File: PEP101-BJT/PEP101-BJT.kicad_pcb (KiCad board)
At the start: 2 copper layers, 45 x 45 mm, 14 parts, among them J1 Screw_Terminal_01x02, J2 Screw_Terminal_01x02, J3 Screw_Terminal_01x02, Q2 MMBT5551L

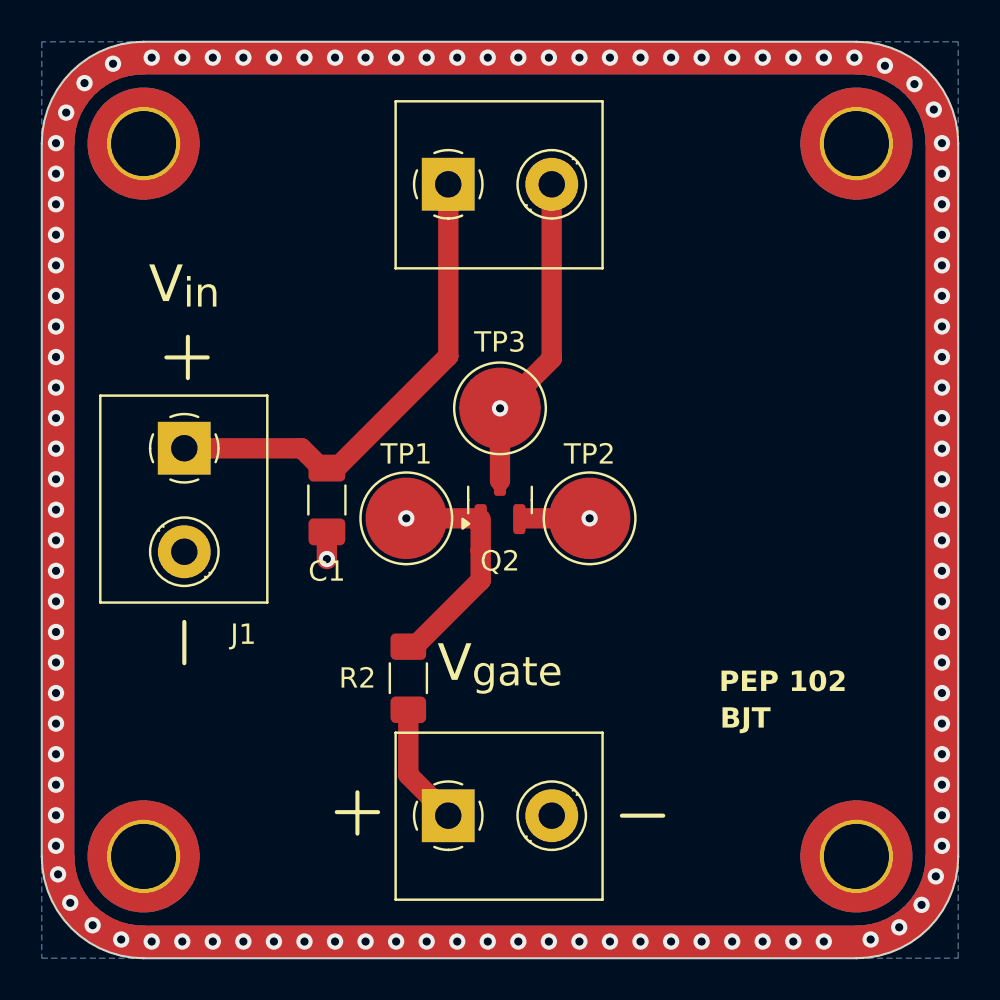
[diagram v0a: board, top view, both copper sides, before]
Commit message: bjt and mosfet need to be redesigned.
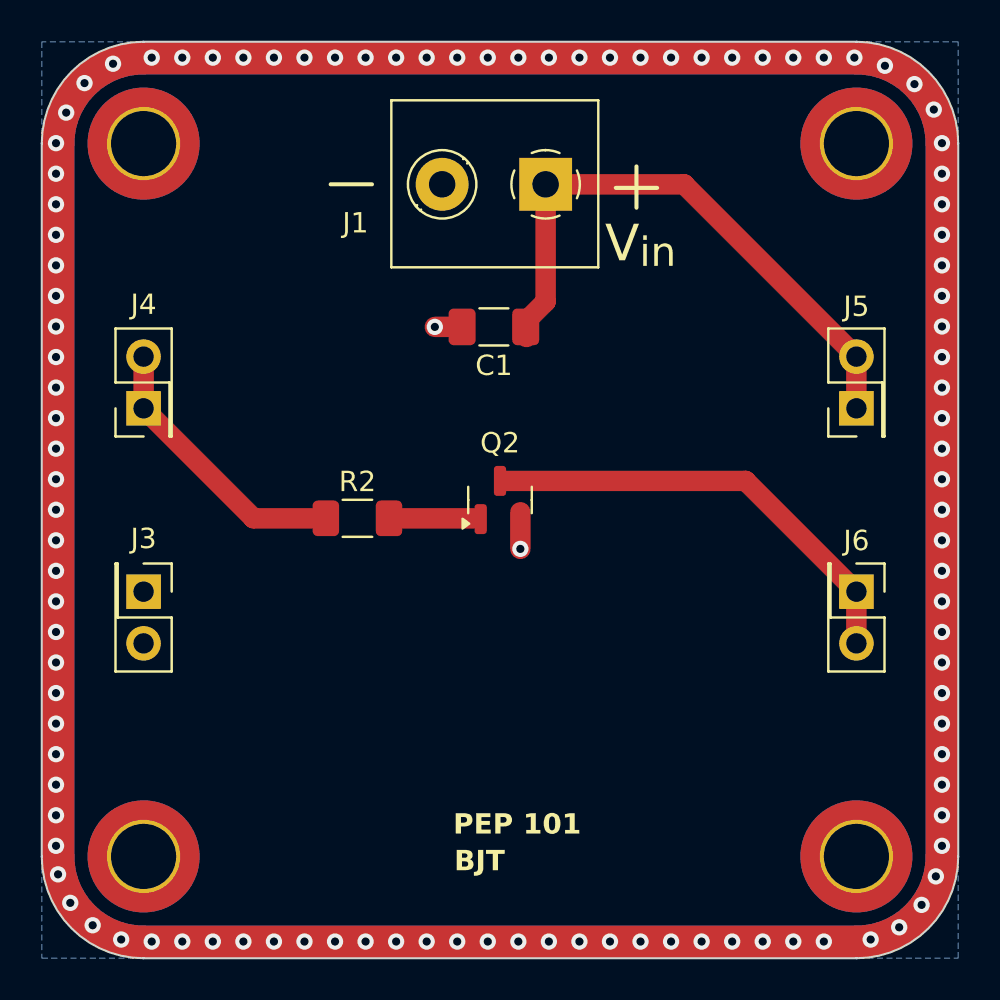
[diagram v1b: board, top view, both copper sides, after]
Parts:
- removed J2: Screw_Terminal_01x02, PEP_library:Screw terminal
- removed REF**: R_silk_symbol, PEP:R_silk_symbol
- removed TP1, TP2, TP3: TestPoint, TestPoint:TestPoint_Pad_D4.0mm
- added J4: Conn_01x02_Pin, Connector_PinHeader_2.54mm:PinHeader_2x01_P2.54mm_Vertical, F.Cu at (105.0, 118.0)
- added J5: Conn_01x02_Pin, Connector_PinHeader_2.54mm:PinHeader_2x01_P2.54mm_Vertical, F.Cu at (140.0, 118.0)
- added J6: Conn_01x02_Pin, Connector_PinHeader_2.54mm:PinHeader_2x01_P2.54mm_Vertical, F.Cu at (140.0, 127.0)
- J3: value Screw_Terminal_01x02 -> Conn_01x02_Pin; footprint PEP_library:TerminalBlock_Phoenix_MKDS-1,5-2-5.08_1x02_P5.08mm_Horizontal -> Connector_PinHeader_2.54mm:PinHeader_2x01_P2.54mm_Vertical
- moved J1 21.7 mm to (122.2, 107.0), turned to 180 degrees
- moved J3 20.7 mm to (105.0, 127.0), turned to -90 degrees
- moved C1 11.8 mm to (122.2, 114.0), turned to 180 degrees
- moved R2 8.24 mm to (115.5, 123.4), turned to 0 degrees
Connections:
- J3 pad 1: BASE -> 0
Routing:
- net BASE: track 5.89 -> 13.9 mm
- net Net-(Q2-B): track 10.7 -> 4.00 mm, vias 1 -> 0
- net Net-(J6-Pin_1): track 15.7 -> 22.1 mm, vias 1 -> 0
- net VCC: track 24.2 -> 29.9 mm
- net 0: track 4.40 -> 3.00 mm
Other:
- board text added: "PEP 101"
- board text removed: "PEP 102"

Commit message: Nova estetika.
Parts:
- added REF**: R_silk_symbol, PEP_library:R_silk_symbol, F.Cu at (110.1, 116.8)
- added REF**: C_silk_symbol, PEP_library:C_silk_symbol, F.Cu at (125.2, 118.8)
- added REF**: NPNsilk, PEP_library:NPNsilk, F.Cu at (123.5, 131.4)
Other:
- board text removed: "BJT"
- board text removed: "PEP 101"
- board text removed: "V_{collector}"
